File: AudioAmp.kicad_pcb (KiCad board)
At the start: 2 copper layers, 145 x 40 mm, 55 parts, among them J1 ACJS-MHOM, J2 ACJS-MHOM, Q1 MJE182G, Q12 MMBT5401, Q13 MMBT5401, Q2 MJE172G, Q3 MMBT5551(RANGE:200-300), Q9 MMBT5551(RANGE:200-300)

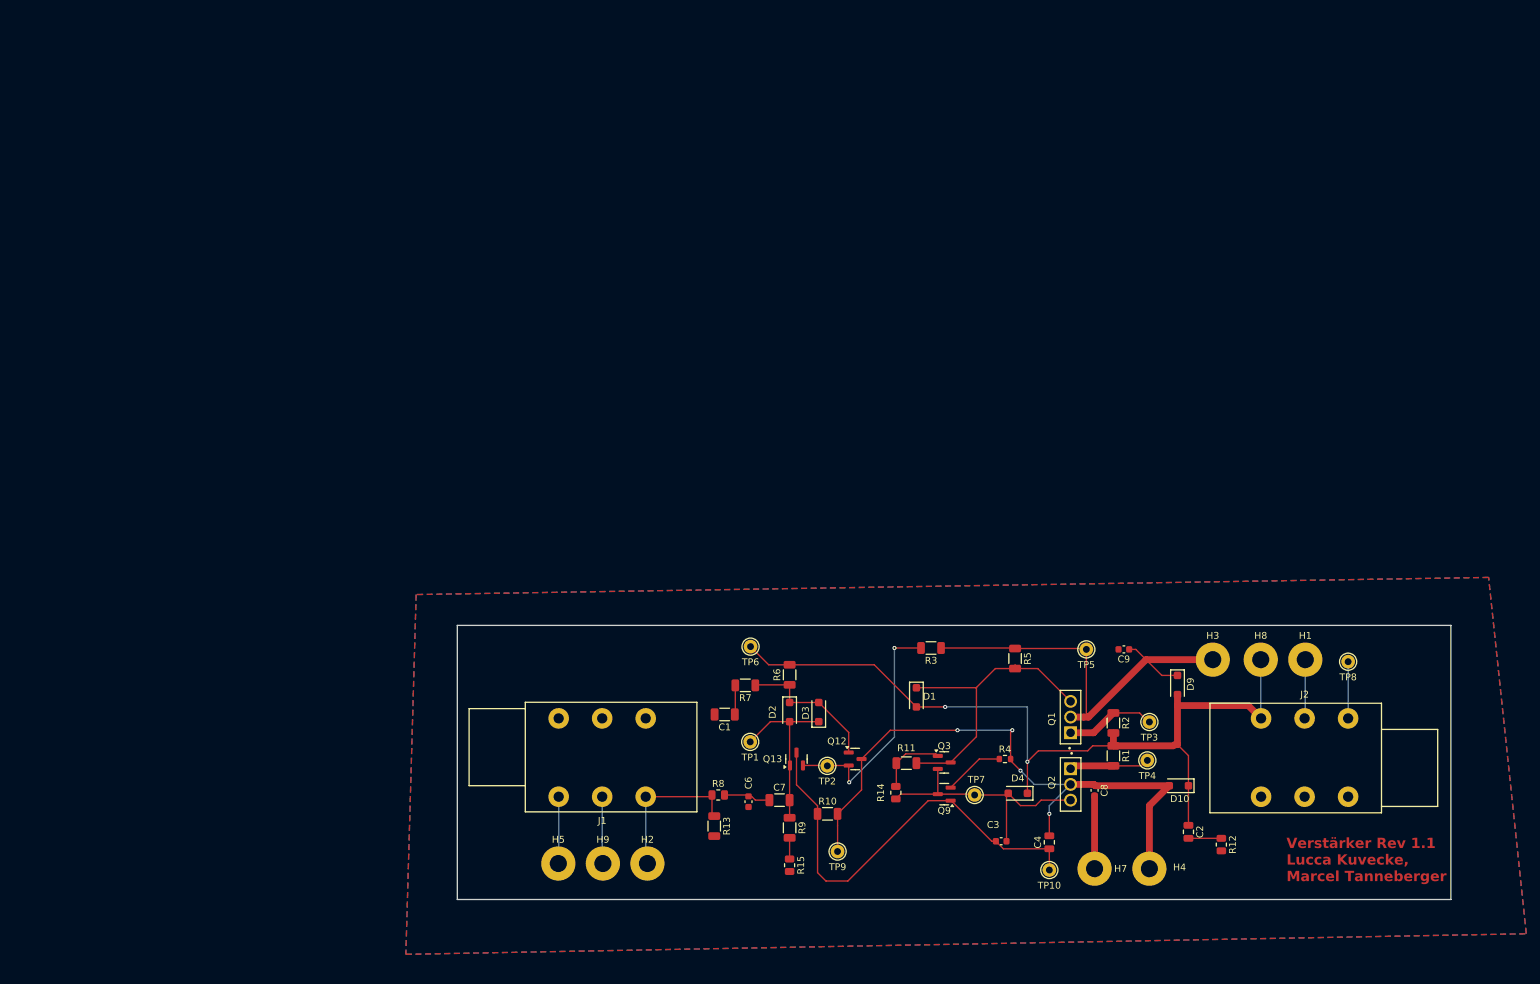
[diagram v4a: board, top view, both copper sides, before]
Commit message: CHA: PCB Testpin zu point, refill GND
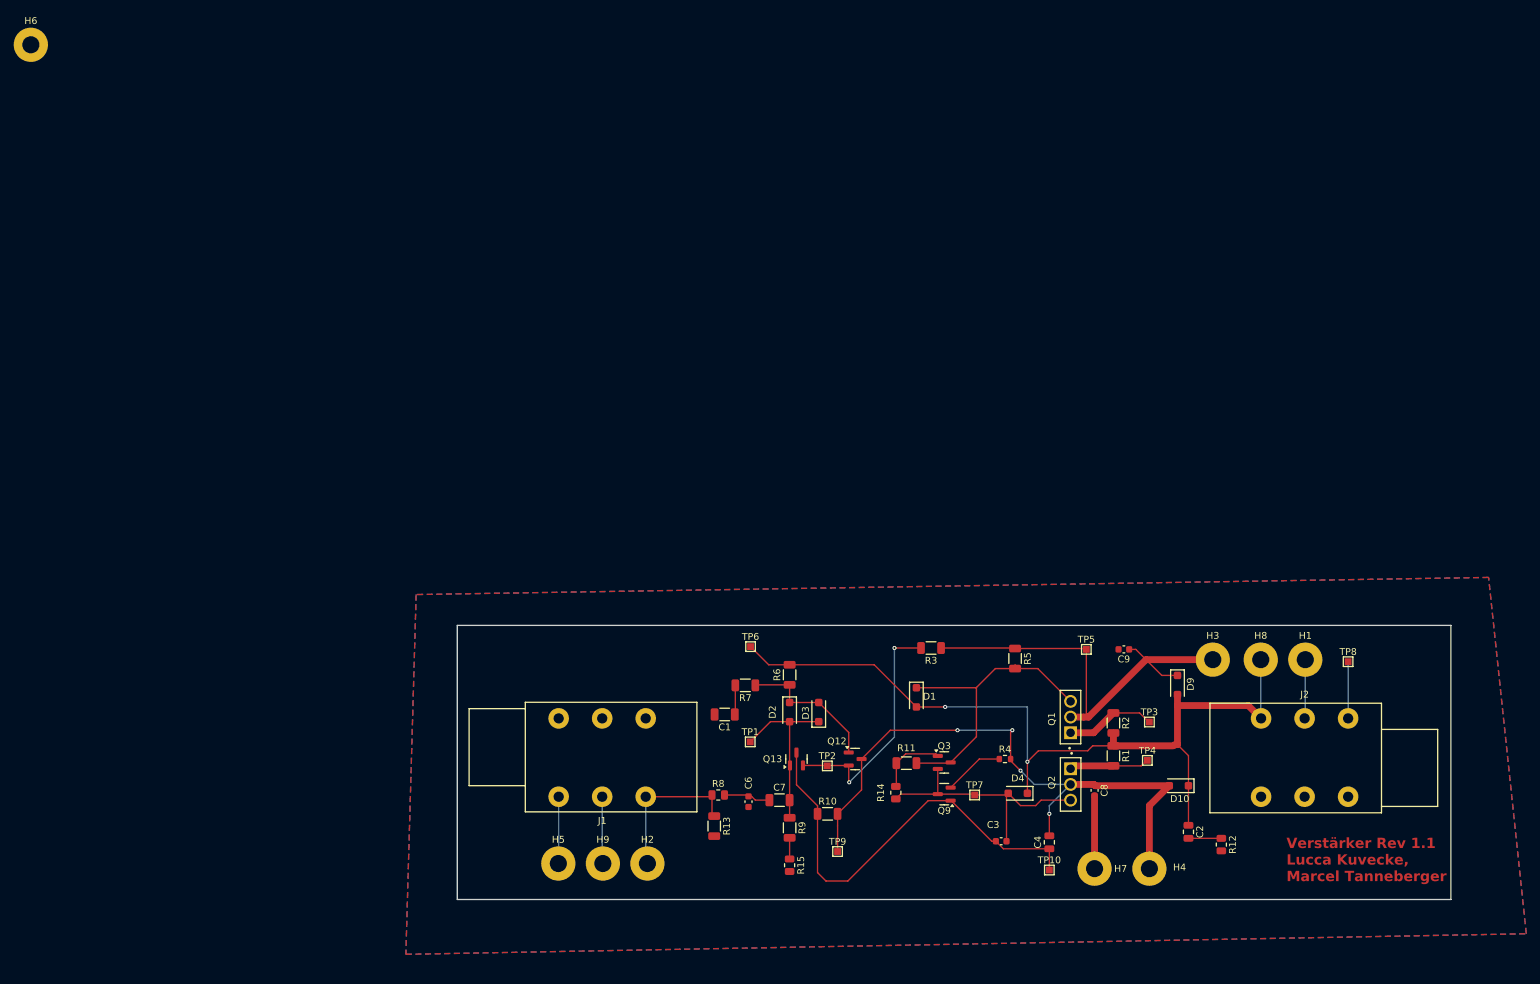
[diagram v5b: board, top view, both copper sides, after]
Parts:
- added H6: VCC _GND, MountingHole:MountingHole_2.5mm_Pad, F.Cu at (2.77, 2.77)
- TP1, TP10, TP2, TP3, TP4, TP5, TP6, TP7, TP8, TP9: footprint Connector_Pin:Pin_D1.0mm_L10.0mm -> TestPoint:TestPoint_Pad_1.0x1.0mm

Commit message: CHA: H6 raus
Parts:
- removed H6: VCC _GND, MountingHole:MountingHole_2.5mm_Pad
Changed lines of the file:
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@@
-		(embedded_fonts no)
-	)
-	(footprint "MountingHole:MountingHole_2.5mm_Pad"
-		(layer "F.Cu")
-		(at 2.775 2.775)
-		(descr "Mounting Hole 2.5mm")
-		(tags "mounting hole 2.5mm")
-		(property "Reference" "H6"
-			(at 0 -3.5 0)
-			(layer "F.SilkS")
-			(effects
-				(font
-					(size 1 1)
-					(thickness 0.15)
-				)
-			)
-		)
-		(property "Value" "VCC _GND"
-			(at 0 3.5 0)
-			(layer "F.Fab")
-			(effects
-				(font
-					(size 1 1)
-					(thickness 0.15)
-				)
-			)
-		)
-		(property "Datasheet" ""
-			(at 0 0 0)
-			(unlocked yes)
-			(layer "F.Fab")
-			(hide yes)
-			(effects
-				(font
-					(size 1.27 1.27)
-					(thickness 0.15)
-				)
-			)
-		)
-		(property "Description" "Mounting Hole with connection"
-			(at 0 0 0)
-			(unlocked yes)
-			(layer "F.Fab")
-			(hide yes)
-			(effects
-				(font
-					(size 1.27 1.27)
-					(thickness 0.15)
-				)
-			)
-		)
-		(property ki_fp_filters "MountingHole*Pad*")
-		(sheetname "/")
-		(sheetfile "AudioAmp.kicad_sch")
-		(attr exclude_from_pos_files exclude_from_bom dnp)
-		(fp_circle
-			(center 0 0)
-			(end 2.5 0)
-			(stroke
-				(width 0.15)
-				(type solid)
-			)
-			(fill no)
-			(layer "Cmts.User")
-		)
-		(fp_circle
-			(center 0 0)
-			(end 2.75 0)
-			(stroke
-				(width 0.05)
-				(type solid)
-			)
-			(fill no)
-			(layer "F.CrtYd")
-		)
-		(fp_text user "${REFERENCE}"
-			(at 0 0 0)
-			(layer "F.Fab")
-			(effects
-				(font
-					(size 1 1)
-					(thickness 0.15)
-				)
-			)
-		)
-		(pad "1" thru_hole circle
-			(at 0 0)
-			(size 5 5)
-			(drill 2.5)
-			(layers "*.Cu" "*.Mask")
-			(remove_unused_layers no)
-			(net 2 "/GND")
-			(pinfunction "1")
-			(pintype "input")
-		)
 		(embedded_fonts no)
 	)

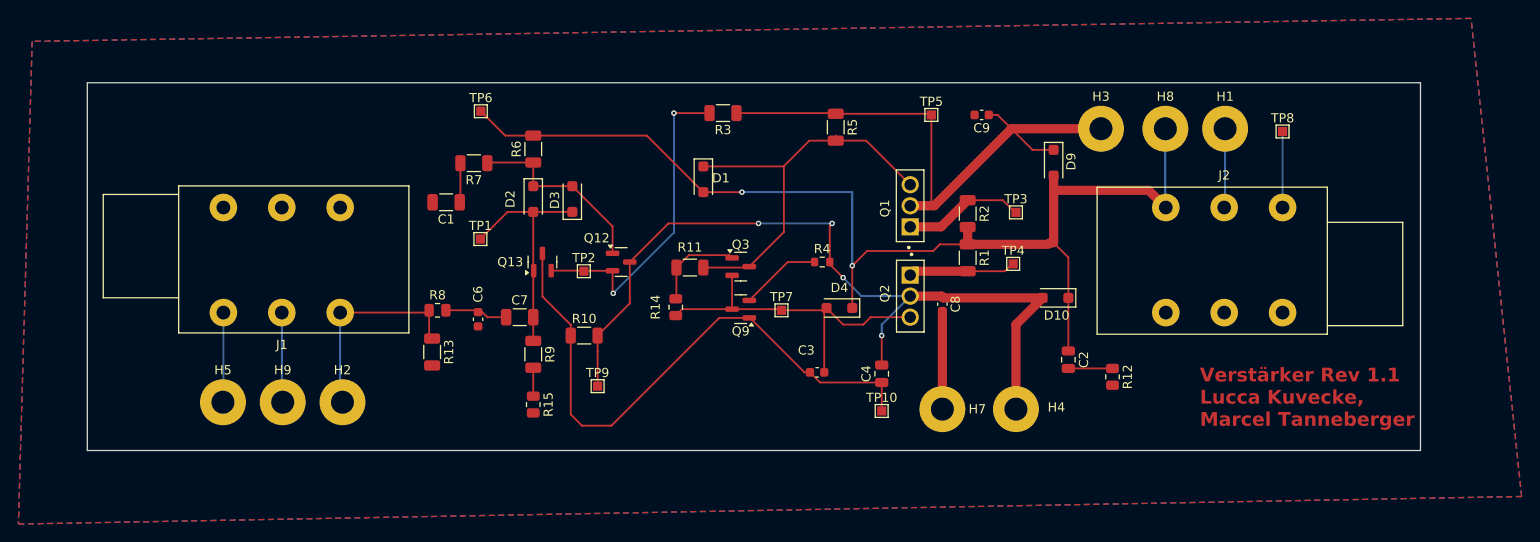
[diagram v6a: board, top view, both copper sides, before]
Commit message: CHA: TP8 changed
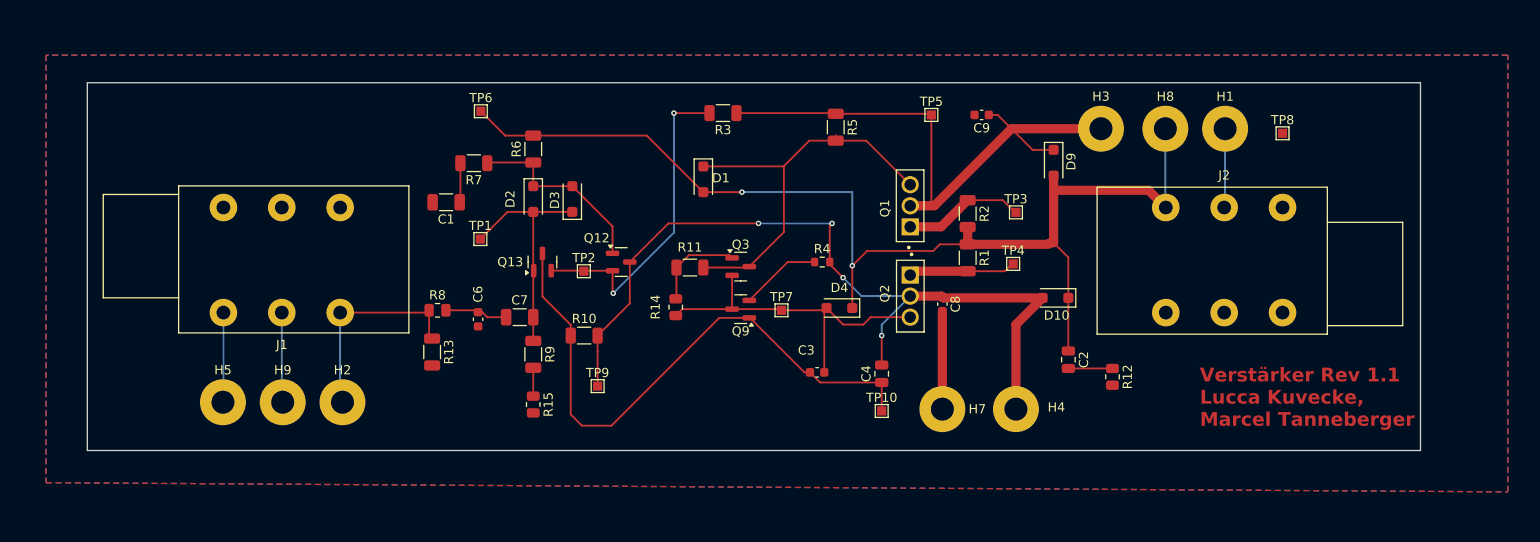
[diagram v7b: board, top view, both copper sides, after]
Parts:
- moved TP8 0.20 mm to (195.0, 93.0)
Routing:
- net /GND: track 28.7 -> 20.4 mm
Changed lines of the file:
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@@
 		)
 	)
-	(footprint "TestPoint:TestPoint_Pad_1.0x1.0mm"
-		(layer "F.Cu")
-		(at 195 92.8)
-		(descr "SMD rectangular pad as test Point, square 1.0mm side length")
-		(tags "test point SMD pad rectangle square")
-		(property "Reference" "TP8"
-			(at 0 -1.448 0)
-			(layer "F.SilkS")
-			(effects
-				(font
-					(size 1 1)
-					(thickness 0.15)
-				)
-			)
-		)
-		(property "Value" "TestPoint"
-			(at 0 1.55 0)
-			(layer "F.Fab")
-			(effects
-				(font
-					(size 1 1)
-					(thickness 0.15)
-				)
-			)
-		)
-		(property "Datasheet" ""
-			(at 0 0 0)
-			(unlocked yes)
-			(layer "F.Fab")
-			(hide yes)
-			(effects
-				(font
-					(size 1.27 1.27)
-					(thickness 0.15)
-				)
-			)
-		)
-		(property "Description" "JIALICHUANG SMT TestPoint"
-			(at 0 0 0)
-			(unlocked yes)
-			(layer "F.Fab")
-			(hide yes)
-			(effects
-				(font
-					(size 1.27 1.27)
-					(thickness 0.15)
-				)
-			)
-		)
-		(property "MPN" "C9900045500"
-			(at 0 0 0)
-			(unlocked yes)
-			(layer "F.Fab")
-			(hide yes)
-			(effects
-				(font
-					(size 1 1)
-					(thickness 0.15)
-				)
-			)
-		)
-		(property ki_fp_filters "Pin* Test*")
-		(sheetname "/")
-		(sheetfile "AudioAmp.kicad_sch")
-		(attr exclude_from_pos_files)
-		(fp_line
-			(start -0.7 -0.7)
-			(end 0.7 -0.7)
-			(stroke
-				(width 0.12)
-				(type solid)
-			)
-			(layer "F.SilkS")
-		)
-		(fp_line
-			(start -0.7 0.7)
-			(end -0.7 -0.7)
-			(stroke
-				(width 0.12)
-				(type solid)
-			)
-			(layer "F.SilkS")
-		)
-		(fp_line
-			(start 0.7 -0.7)
-			(end 0.7 0.7)
-			(stroke
-				(width 0.12)
-				(type solid)
-			)
-			(layer "F.SilkS")
-		)
-		(fp_line
-			(start 0.7 0.7)
-			(end -0.7 0.7)
-			(stroke
-				(width 0.12)
-				(type solid)
-			)
-			(layer "F.SilkS")
-		)
-		(fp_line
-			(start -1 -1)
-			(end -1 1)
-			(stroke
-				(width 0.05)
-				(type solid)
-			)
-			(layer "F.CrtYd")
-		)
-		(fp_line
-			(start -1 -1)
-			(end 1 -1)
-			(stroke
-				(width 0.05)
-				(type solid)
-			)
-			(layer "F.CrtYd")
-		)
-		(fp_line
-			(start 1 1)
-			(end -1 1)
-			(stroke
-				(width 0.05)
-				(type solid)
-			)
-			(layer "F.CrtYd")
-		)
-		(fp_line
-			(start 1 1)
-			(end 1 -1)
-			(stroke
-				(width 0.05)
-				(type solid)
-			)
-			(layer "F.CrtYd")
-		)
-		(fp_text user "${REFERENCE}"
-			(at 0 -1.45 0)
-			(layer "F.Fab")
-			(effects
-				(font
-					(size 1 1)
-					(thickness 0.15)
-				)
-			)
-		)
-		(pad "1" smd rect
-			(at 0 0)
-			(size 1 1)
-			(layers "F.Cu" "F.Mask")
-			(net 2 "/GND")
-			(pinfunction "1")
-			(pintype "passive")
-		)
-		(embedded_fonts no)
-	)
 	(footprint "Importierte Footprints:TO229P780X300X1364-3"
 		(layer "F.Cu")
@@
 		)
 	)
+	(footprint "TestPoint:TestPoint_Pad_1.0x1.0mm"
+		(layer "F.Cu")
+		(at 195 93)
+		(descr "SMD rectangular pad as test Point, square 1.0mm side length")
+		(tags "test point SMD pad rectangle square")
+		(property "Reference" "TP8"
+			(at 0 -1.448 0)
+			(layer "F.SilkS")
+			(effects
+				(font
+					(size 1 1)
+					(thickness 0.15)
+				)
+			)
+		)
+		(property "Value" "TestPoint"
+			(at 0 1.55 0)
+			(layer "F.Fab")
+			(effects
+				(font
+					(size 1 1)
+					(thickness 0.15)
+				)
+			)
+		)
+		(property "Datasheet" ""
+			(at 0 0 0)
+			(unlocked yes)
+			(layer "F.Fab")
+			(hide yes)
+			(effects
+				(font
+					(size 1.27 1.27)
+					(thickness 0.15)
+				)
+			)
+		)
+		(property "Description" "JIALICHUANG SMT TestPoint"
+			(at 0 0 0)
+			(unlocked yes)
+			(layer "F.Fab")
+			(hide yes)
+			(effects
+				(font
+					(size 1.27 1.27)
+					(thickness 0.15)
+				)
+			)
+		)
+		(property "MPN" "C9900045500"
+			(at 0 0 0)
+			(unlocked yes)
+			(layer "F.Fab")
+			(hide yes)
+			(effects
+				(font
+					(size 1 1)
+					(thickness 0.15)
+				)
+			)
+		)
+		(property ki_fp_filters "Pin* Test*")
+		(sheetname "/")
+		(sheetfile "AudioAmp.kicad_sch")
+		(attr exclude_from_pos_files)
+		(fp_line
+			(start -0.7 -0.7)
+			(end 0.7 -0.7)
+			(stroke
+				(width 0.12)
+				(type solid)
+			)
+			(layer "F.SilkS")
+		)
+		(fp_line
+			(start -0.7 0.7)
+			(end -0.7 -0.7)
+			(stroke
+				(width 0.12)
+				(type solid)
+			)
+			(layer "F.SilkS")
+		)
+		(fp_line
+			(start 0.7 -0.7)
+			(end 0.7 0.7)
+			(stroke
+				(width 0.12)
+				(type solid)
+			)
+			(layer "F.SilkS")
+		)
+		(fp_line
+			(start 0.7 0.7)
+			(end -0.7 0.7)
+			(stroke
+				(width 0.12)
+				(type solid)
+			)
+			(layer "F.SilkS")
+		)
+		(fp_line
+			(start -1 -1)
+			(end -1 1)
+			(stroke
+				(width 0.05)
+				(type solid)
+			)
+			(layer "F.CrtYd")
+		)
+		(fp_line
+			(start -1 -1)
+			(end 1 -1)
+			(stroke
+				(width 0.05)
+				(type solid)
+			)
+			(layer "F.CrtYd")
+		)
+		(fp_line
+			(start 1 1)
+			(end -1 1)
+			(stroke
+				(width 0.05)
+				(type solid)
+			)
+			(layer "F.CrtYd")
+		)
+		(fp_line
+			(start 1 1)
+			(end 1 -1)
+			(stroke
+				(width 0.05)
+				(type solid)
+			)
+			(layer "F.CrtYd")
+		)
+		(fp_text user "${REFERENCE}"
+			(at 0 -1.45 0)
+			(layer "F.Fab")
+			(effects
+				(font
+					(size 1 1)
+					(thickness 0.15)
+				)
+			)
+		)
+		(pad "1" smd rect
+			(at 0 0)
+			(size 1 1)
+			(layers "F.Cu" "F.Mask")
+			(net 2 "/GND")
+			(pinfunction "1")
+			(pintype "passive")
+		)
+		(embedded_fonts no)
+	)
 	(footprint "Capacitor_SMD:C_0805_2012Metric"
 		(layer "F.Cu")
@@
 	)
 	(segment
-		(start 195 92.8)
-		(end 195 101.07)
-		(width 0.2)
-		(layer "B.Cu")
-		(net 2)
-	)
-	(segment
 		(start 79.8 122.2)
 		(end 79.75 122.25)
@@
 		(net_name "/GND")
 		(layers "F.Cu" "B.Cu")
-		(hatch full 0.5)
+		(hatch edge 0.5)
 		(connect_pads
 			(clearance 0.5)
@@
 		(polygon
 			(pts
-				(xy 59 83) (xy 57.5 135.5) (xy 221 132.5) (xy 215.5 80.5)
+				(xy 60.5 84.5) (xy 60.5 131) (xy 219.5 132) (xy 219.5 84.5)
 			)
 		)

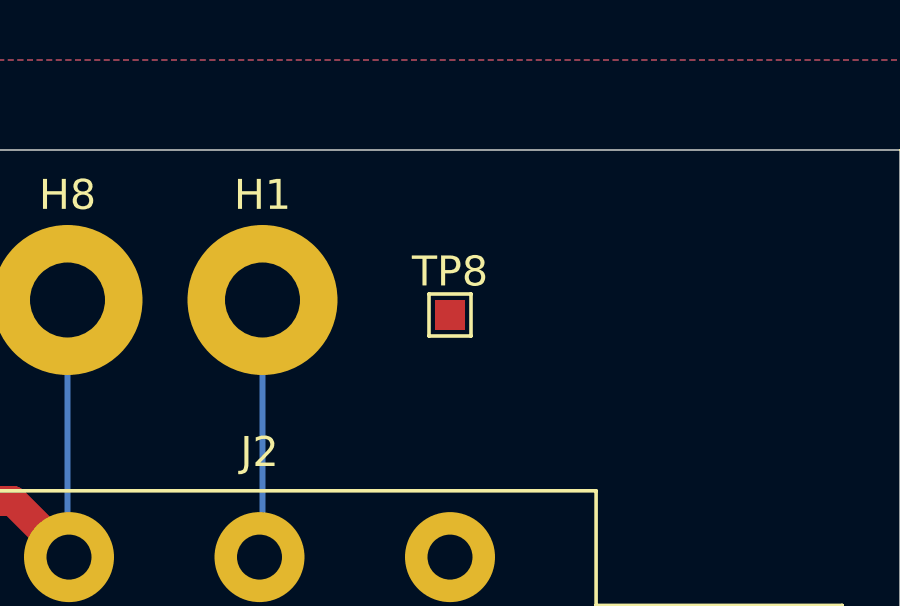
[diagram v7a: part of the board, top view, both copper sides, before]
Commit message: CHA: PCB Testpad breiter
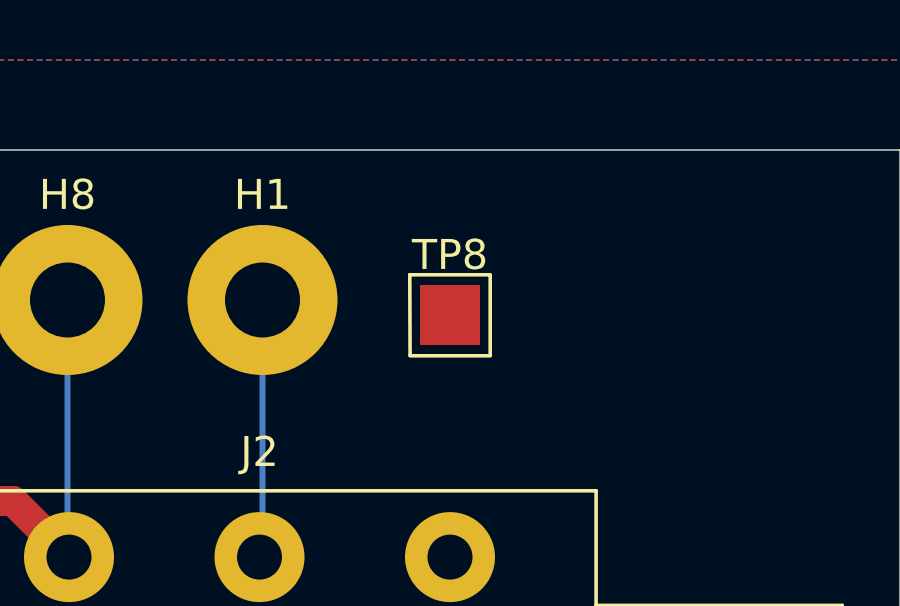
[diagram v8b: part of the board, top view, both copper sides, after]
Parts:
- TP8: footprint TestPoint:TestPoint_Pad_1.0x1.0mm -> TestPoint:TestPoint_Pad_2.0x2.0mm
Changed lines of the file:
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@@
 		)
 	)
-	(footprint "TestPoint:TestPoint_Pad_1.0x1.0mm"
+	(footprint "TestPoint:TestPoint_Pad_2.0x2.0mm"
 		(layer "F.Cu")
 		(at 195 93)
-		(descr "SMD rectangular pad as test Point, square 1.0mm side length")
+		(descr "SMD rectangular pad as test Point, square 2.0mm side length")
 		(tags "test point SMD pad rectangle square")
 		(property "Reference" "TP8"
-			(at 0 -1.448 0)
+			(at 0 -1.998 0)
 			(layer "F.SilkS")
 			(effects
@@
 		)
 		(property "Value" "TestPoint"
-			(at 0 1.55 0)
+			(at 0 2.35 0)
 			(layer "F.Fab")
 			(effects
@@
 			)
 		)
-		(property "MPN" "C9900045500"
-			(at 0 0 0)
-			(unlocked yes)
-			(layer "F.Fab")
-			(hide yes)
-			(effects
-				(font
-					(size 1 1)
-					(thickness 0.15)
-				)
-			)
-		)
 		(property ki_fp_filters "Pin* Test*")
 		(sheetname "/")
@@
 		(attr exclude_from_pos_files)
 		(fp_line
-			(start -0.7 -0.7)
-			(end 0.7 -0.7)
+			(start -1.34051 -1.34)
+			(end 1.33 -1.34)
 			(stroke
 				(width 0.12)
@@
 		)
 		(fp_line
-			(start -0.7 0.7)
-			(end -0.7 -0.7)
+			(start -1.33 1.34)
+			(end -1.34051 -1.34)
 			(stroke
 				(width 0.12)
@@
 		)
 		(fp_line
-			(start 0.7 -0.7)
-			(end 0.7 0.7)
+			(start 1.34 -1.34)
+			(end 1.34 1.33)
 			(stroke
 				(width 0.12)
@@
 		)
 		(fp_line
-			(start 0.7 0.7)
-			(end -0.7 0.7)
+			(start 1.34 1.36)
+			(end -1.329922 1.36)
 			(stroke
 				(width 0.12)
@@
 		)
 		(fp_line
-			(start -1 -1)
-			(end -1 1)
+			(start -1.5 -1.5)
+			(end -1.5 1.5)
 			(stroke
 				(width 0.05)
@@
 		)
 		(fp_line
-			(start -1 -1)
-			(end 1 -1)
+			(start -1.5 -1.5)
+			(end 1.5 -1.5)
 			(stroke
 				(width 0.05)
@@
 		)
 		(fp_line
-			(start 1 1)
-			(end -1 1)
+			(start 1.5 1.5)
+			(end -1.5 1.5)
 			(stroke
 				(width 0.05)
@@
 		)
 		(fp_line
-			(start 1 1)
-			(end 1 -1)
+			(start 1.5 1.5)
+			(end 1.5 -1.5)
 			(stroke
 				(width 0.05)
@@
 		)
 		(fp_text user "${REFERENCE}"
-			(at 0 -1.45 0)
+			(at 0 -2 0)
 			(layer "F.Fab")
 			(effects
@@
 		(pad "1" smd rect
 			(at 0 0)
-			(size 1 1)
+			(size 2 2)
 			(layers "F.Cu" "F.Mask")
 			(net 2 "/GND")
